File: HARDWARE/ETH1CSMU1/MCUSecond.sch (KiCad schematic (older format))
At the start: 30 parts, among them J201 Conn_02x05, U201 24LC08, U202 STM32F746ZGTx, X201 CRYSTAL_4PIN

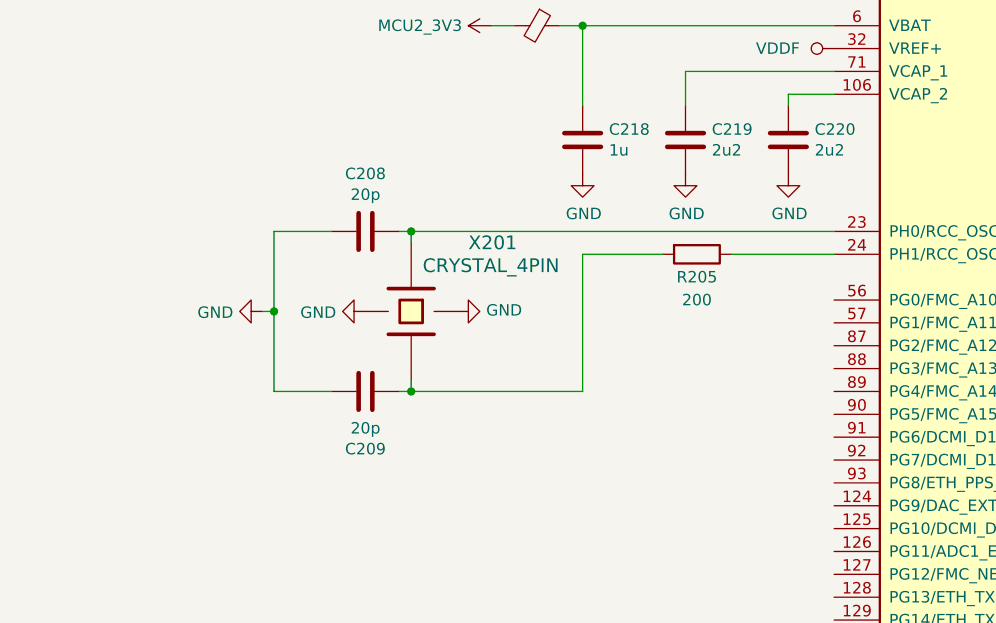
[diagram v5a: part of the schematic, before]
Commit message: Redesigned feedback circuit.
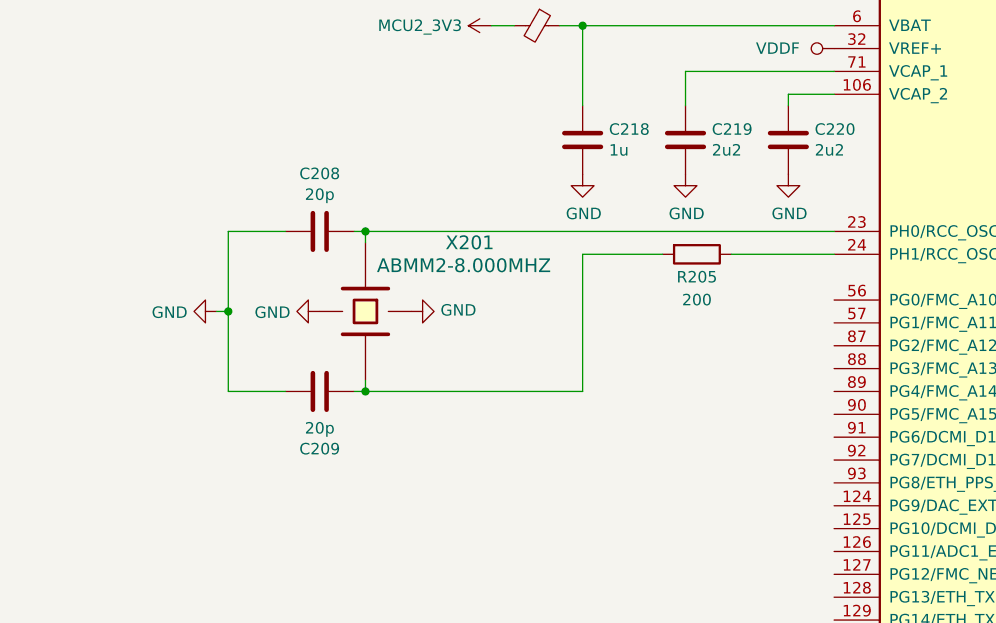
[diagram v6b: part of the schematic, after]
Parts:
- X201: value CRYSTAL_4PIN -> ABMM2-8.000MHZ
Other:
- moved on the sheet: C208, C209, X201
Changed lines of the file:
@@
 L crystal_local:CRYSTAL_4PIN X201
 U 1 1 5BCFF872
-P 2200 3500
-F 0 "X201" V 1900 3750 60  0000 L CNN
-F 1 "CRYSTAL_4PIN" V 2000 3550 60  0000 L CNN
-F 2 "" H 2200 3500 60  0001 C CNN
-F 3 "" H 2200 3500 60  0000 C CNN
-	1    2200 3500
+P 2000 3500
+F 0 "X201" V 1700 3850 60  0000 L CNN
+F 1 "ABMM2-8.000MHZ" V 1800 3550 60  0000 L CNN
+F 2 "" H 2000 3500 60  0001 C CNN
+F 3 "" H 2000 3500 60  0000 C CNN
+	1    2000 3500
 	0    1    1    0
 $EndComp
 Wire Wire Line
-	2200 3200 2200 3150
-Wire Wire Line
-	2200 3800 2200 3850
-Wire Wire Line
-	2200 3850 2950 3850
+	2000 3200 2000 3150
+Wire Wire Line
+	2000 3800 2000 3850
 $Comp
 L Device:C C208
 U 1 1 5BD0316A
-P 2000 3150
-F 0 "C208" V 1748 3150 50  0000 C CNN
-F 1 "20p" V 1839 3150 50  0000 C CNN
-F 2 "Capacitors_SMD:C_0603" H 2038 3000 50  0001 C CNN
-F 3 "~" H 2000 3150 50  0001 C CNN
-	1    2000 3150
+P 1800 3150
+F 0 "C208" V 1548 3150 50  0000 C CNN
+F 1 "20p" V 1639 3150 50  0000 C CNN
+F 2 "Capacitors_SMD:C_0603" H 1838 3000 50  0001 C CNN
+F 3 "~" H 1800 3150 50  0001 C CNN
+	1    1800 3150
 	0    1    1    0
 $EndComp
 Wire Wire Line
-	2150 3150 2200 3150
-Connection ~ 2200 3150
+	1950 3150 2000 3150
+Connection ~ 2000 3150
 $Comp
 L Device:C C209
 U 1 1 5BD03A9C
-P 2000 3850
-F 0 "C209" V 2252 3850 50  0000 C CNN
-F 1 "20p" V 2161 3850 50  0000 C CNN
-F 2 "Capacitors_SMD:C_0603" H 2038 3700 50  0001 C CNN
-F 3 "~" H 2000 3850 50  0001 C CNN
-	1    2000 3850
+P 1800 3850
+F 0 "C209" V 2052 3850 50  0000 C CNN
+F 1 "20p" V 1961 3850 50  0000 C CNN
+F 2 "Capacitors_SMD:C_0603" H 1838 3700 50  0001 C CNN
+F 3 "~" H 1800 3850 50  0001 C CNN
+	1    1800 3850
 	0    -1   1    0
 $EndComp
 Wire Wire Line
-	2150 3850 2200 3850
-Connection ~ 2200 3850
-Wire Wire Line
-	1850 3850 1600 3850
-Wire Wire Line
-	1600 3850 1600 3500
-Wire Wire Line
-	1600 3150 1850 3150
-Wire Wire Line
-	1550 3500 1600 3500
-Connection ~ 1600 3500
-Wire Wire Line
-	1600 3500 1600 3150
+	1950 3850 2000 3850
+Connection ~ 2000 3850
+Wire Wire Line
+	1650 3850 1400 3850
+Wire Wire Line
+	1400 3850 1400 3500
+Wire Wire Line
+	1400 3150 1650 3150
+Wire Wire Line
+	1350 3500 1400 3500
+Connection ~ 1400 3500
+Wire Wire Line
+	1400 3500 1400 3150
 $Comp
 L Connector_Generic:Conn_02x05_Odd_Even J201
@@
 L power:GND #PWR0213
 U 1 1 5BED55F5
-P 2000 3500
-F 0 "#PWR0213" H 2000 3250 50  0001 C CNN
-F 1 "GND" V 2005 3372 50  0000 R CNN
-F 2 "" H 2000 3500 50  0001 C CNN
-F 3 "" H 2000 3500 50  0001 C CNN
-	1    2000 3500
+P 1800 3500
+F 0 "#PWR0213" H 1800 3250 50  0001 C CNN
+F 1 "GND" V 1805 3372 50  0000 R CNN
+F 2 "" H 1800 3500 50  0001 C CNN
+F 3 "" H 1800 3500 50  0001 C CNN
+	1    1800 3500
 	0    1    1    0
 $EndComp
@@
 L power:GND #PWR0216
 U 1 1 5BED56C8
-P 2400 3500
-F 0 "#PWR0216" H 2400 3250 50  0001 C CNN
-F 1 "GND" V 2405 3372 50  0000 R CNN
-F 2 "" H 2400 3500 50  0001 C CNN
-F 3 "" H 2400 3500 50  0001 C CNN
-	1    2400 3500
+P 2200 3500
+F 0 "#PWR0216" H 2200 3250 50  0001 C CNN
+F 1 "GND" V 2205 3372 50  0000 R CNN
+F 2 "" H 2200 3500 50  0001 C CNN
+F 3 "" H 2200 3500 50  0001 C CNN
+	1    2200 3500
 	0    -1   -1   0
 $EndComp
@@
 L power:GND #PWR0212
 U 1 1 5BED5723
-P 1550 3500
-F 0 "#PWR0212" H 1550 3250 50  0001 C CNN
-F 1 "GND" V 1555 3372 50  0000 R CNN
-F 2 "" H 1550 3500 50  0001 C CNN
-F 3 "" H 1550 3500 50  0001 C CNN
-	1    1550 3500
+P 1350 3500
+F 0 "#PWR0212" H 1350 3250 50  0001 C CNN
+F 1 "GND" V 1355 3372 50  0000 R CNN
+F 2 "" H 1350 3500 50  0001 C CNN
+F 3 "" H 1350 3500 50  0001 C CNN
+	1    1350 3500
 	0    1    1    0
 $EndComp
@@
 	8350 8900 8350 8850
 Connection ~ 8450 8900
-Wire Wire Line
-	2200 3150 4050 3150
 Wire Wire Line
 	2950 3250 2950 3850
@@
 	1    0    0    -1
 $EndComp
+Wire Wire Line
+	2000 3850 2950 3850
+Wire Wire Line
+	2000 3150 4050 3150
 $EndSCHEMATC

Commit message: Schematic development
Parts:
- renumbered C202 to C201, C208 to C202, C209 to C203, C218 to C204, C219 to C205, C220 to C206, C212 to C207, C213 to C208, C201 to C209, C203 to C210, C204 to C211, C205 to C212, C206 to C213, C207 to C214, C210 to C215, C211 to C216, C214 to C217, C215 to C218, C216 to C219, C217 to C220, R205 to R204
